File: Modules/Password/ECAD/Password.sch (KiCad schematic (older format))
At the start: 22 parts, among them J1 comm_header, J2 prog_header, SW1 Letter_1_Up, SW10 Letter_5_Down, SW11 Submit, SW2 Letter_1_Down, SW3 Letter_2_Up, SW4 Letter_2_Down, SW5 Letter_3_Up, SW6 Letter_3_Down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

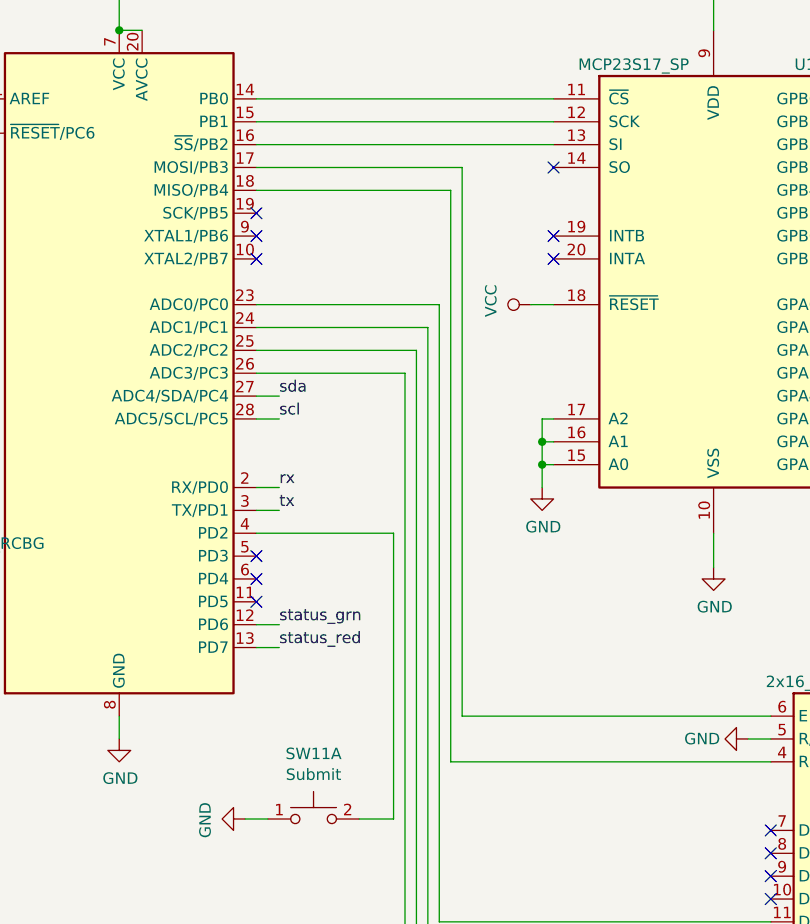
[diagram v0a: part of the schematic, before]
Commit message: Added MISO connection from I/O-expander
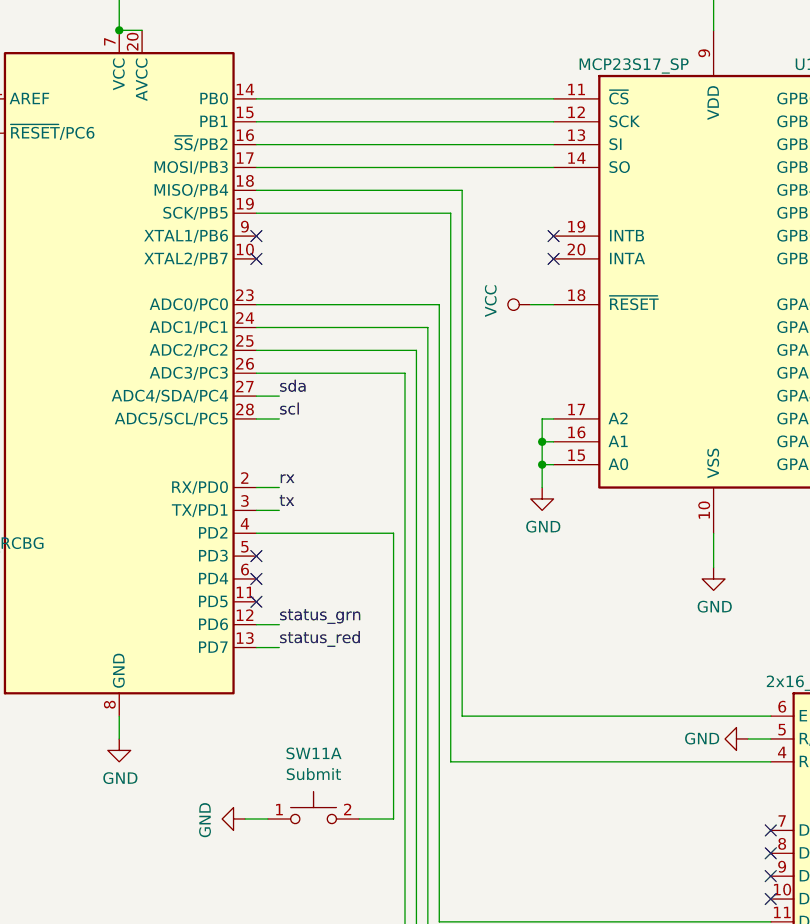
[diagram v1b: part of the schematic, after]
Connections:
- net at U2.17 (MOSI/PB3): now also U1.14 (SO); no longer DS1.6 (E)
- net at U2.18 (MISO/PB4): now also DS1.6 (E); no longer DS1.4 (RS)
- net at U2.19 (SCK/PB5): now also DS1.4 (RS)
- no-connect marks 21 -> 19
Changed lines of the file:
@@
 EESchema Schematic File Version 4
 LIBS:Password-cache
-LIBS:NeedyVentingGas-cache
 EELAYER 29 0
 EELAYER END
@@
 Text Label 2950 4550 3    50   ~ 0
 status_red
-NoConn ~ 4400 2550
 NoConn ~ 4400 2650
 NoConn ~ 4400 2750
@@
 	6650 4750 5300 4750
 Wire Wire Line
-	5300 4750 5300 2350
-Wire Wire Line
-	5300 2350 4400 2350
-Wire Wire Line
-	4400 2450 5250 2450
-Wire Wire Line
-	5250 2450 5250 4950
+	5300 4750 5300 2450
+Wire Wire Line
+	5300 2450 4400 2450
+Wire Wire Line
+	4400 2550 5250 2550
 Wire Wire Line
 	5250 4950 6650 4950
@@
 Wire Wire Line
 	4400 2250 5700 2250
-NoConn ~ 5700 2350
 $Comp
 L power:VCC #PWR02
@@
 Wire Wire Line
 	9700 4000 9700 3650
+Wire Wire Line
+	5250 2550 5250 4950
+Wire Wire Line
+	5700 2350 4400 2350
 $EndSCHEMATC

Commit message: Added polyfuses to all modules
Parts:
- added F1: Polyfuse, symbol Device:Polyfuse
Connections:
- net VCC: now also F1.1; no longer J1.4 (Pin_4), J2.1 (Pin_1)
- new net UVCC: F1.2, J1.4 (Pin_4), J2.1 (Pin_1)
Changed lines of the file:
@@
 L power:VCC #PWR08
 U 1 1 5F5DC5B2
-P 1400 3350
-F 0 "#PWR08" H 1400 3200 50  0001 C CNN
-F 1 "VCC" V 1418 3477 50  0000 L CNN
-F 2 "" H 1400 3350 50  0001 C CNN
-F 3 "" H 1400 3350 50  0001 C CNN
-	1    1400 3350
-	0    -1   -1   0
-$EndComp
-$Comp
-L power:VCC #PWR012
-U 1 1 5F820F96
-P 1400 3950
-F 0 "#PWR012" H 1400 3800 50  0001 C CNN
-F 1 "VCC" V 1418 4077 50  0000 L CNN
-F 2 "" H 1400 3950 50  0001 C CNN
-F 3 "" H 1400 3950 50  0001 C CNN
-	1    1400 3950
-	0    -1   -1   0
+P 2300 3000
+F 0 "#PWR08" H 2300 2850 50  0001 C CNN
+F 1 "VCC" V 2318 3127 50  0000 L CNN
+F 2 "" H 2300 3000 50  0001 C CNN
+F 3 "" H 2300 3000 50  0001 C CNN
+	1    2300 3000
+	0    1    1    0
 $EndComp
 $Comp
@@
 Wire Wire Line
 	5700 2350 4400 2350
+$Comp
+L Device:Polyfuse F1
+U 1 1 5F922822
+P 2050 3000
+F 0 "F1" V 1825 3000 50  0000 C CNN
+F 1 "Polyfuse" V 1916 3000 50  0000 C CNN
+F 2 "" H 2100 2800 50  0001 L CNN
+F 3 "~" H 2050 3000 50  0001 C CNN
+	1    2050 3000
+	0    1    1    0
+$EndComp
+Text Label 1400 3950 2    50   ~ 0
+UVCC
+Text Label 1400 3350 2    50   ~ 0
+UVCC
+Text Label 1800 3000 2    50   ~ 0
+UVCC
+Wire Wire Line
+	1800 3000 1900 3000
+Wire Wire Line
+	2200 3000 2300 3000
 $EndSCHEMATC
